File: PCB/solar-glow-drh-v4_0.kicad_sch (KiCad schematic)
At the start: 73 parts, among them J1 UPDI hdr, Q2 BSS138LT1G, SW2 LED master, U1 AVR64EA28 (VQFN28), U3 ADXL367, U5 NT3H2211, U6 TPS22917, U7 MB85RC512TY, U8 AEM10300, U9 TPS7A0233 (SOT23-5*)

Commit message: The fab package now says which board it is and how it is plated
Every one of the ten gerbers carried `%TF.ProjectId,solar-glow-drh-v4_0,<guid>,rev?*%`,
both .gbrjob files read "Revision": "rev?", and the stackup declared
`copper_finish "None"` -- on a board whose single most consequential fab instruction is
ENIG plus selective hard gold. The panel set was identical. Nothing failed: the fields
were simply blank, and blank is what a CAM operator reads when two zips from the same
project land in the same week.

The cause was one absence. The board had NO title block at all -- GetTitleBlock() returned
title, revision, date and company all empty -- and the schematic had none either.

  board + schematic: title block added (title / date / rev v4.0 / company)
  board stackup:     copper_finish "None" -> "ENIG"

Verified by plotting gerbers locally and reading back what the fab actually receives,
rather than trusting the edit:

  before   ProjectId ... rev?    Finish: None
  after    ProjectId ... v4.0    Finish: ENIG

CHECK [18] GATES BOTH, and gates the revision AGAINST THE FILENAME rather than a constant:
`...-v4_0.kicad_pcb` -> `v4.0`. The filename is already this project's revision of record
and PCB/ holds exactly one board, so a v5 rename now fails this check until the title
block follows it. Negative-tested three ways -- clean on the fixed board, 2 errors on the
exact pre-fix state (blank rev + finish None), 1 error on a rev/filename mismatch -- with
the board restored byte-identical afterward.

ON FINISH, and why ENIG alone is the right value: `copper_finish` is one field and cannot
express "ENIG plus selective hard gold on a named set of pads". ENIG is the base finish and
belongs there; the gold set lives where it can be DRAWN and GATED -- the User.1 plating
artwork generated by scripts/mask_art.py and checked by [14]. Check [18] only insists the
field is not blank, because the moment it tries to encode the special request it becomes a
second home for it.

Also cor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
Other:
- company: (none) -> Devin R. Horowitz
- title: (none) -> SOLAR-GLOW · DRH
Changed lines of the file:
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@@
 	(generator_version "10.0")
 	(paper "A4")
+	(title_block
+		(title "SOLAR-GLOW · DRH")
+		(date "2026-08-04")
+		(rev "v4.0")
+		(company "Devin R. Horowitz")
+	)
 	(no_connect
 		(at 410.21 139.7)

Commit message: The supercap lands pointed at a library that does not exist
SC1-SC4 linked to `Downloads:SCHURTER_SCPC_*` in BOTH the board and the schematic.
PCB/fp-lib-table registers exactly one library, `solarglow`. So the link never
resolved, "Update Footprints from Library" had nothing valid to pull, and the
corrected footprints in PCB/solarglow.pretty/ were unreachable from the board.

That is why correcting the library never reached the board, and why the land is
still wrong on three of four caps.

RELINKED, board and schematic together so schematic parity holds:
  SC1, SC3  Downloads:SCHURTER_SCPC_SS17      -> solarglow:SCHURTER_SCPC_SS17
  SC2, SC4  Downloads:SCHURTER_SCPC_WS17-mod2 -> solarglow:SCHURTER_SCPC_WS17
(`WS17-mod2` has no library counterpart; WS17 is the datasheet-correct land.)
Relinking moves NO copper -- the embedded pads stay until KiCad is told to update.

THE LIBRARY FOOTPRINTS WERE NOT SAFE TO LINK, and this fixes that. They were pad
geometry references, not usable footprints. Each gap would have bitten on the first
"Update Footprints from Library":

  - pads carried F.Paste. The board's carry B.Cu + B.Mask only, deliberately: these
    are hand-soldered under-body lands and PCB/README.md:497 warns that reflowing
    paste under them is "enough solder volume to float the part". Removed.
  - `(attr smd)` only, where the board has `exclude_from_pos_files exclude_from_bom`.
    Updating would have put four supercaps back into the CPL and the BOM -- the exact
    defect check [15] was written after. Set to match.
  - no 3D model. Updating would have stripped SCHURTER_SCPC_*.step, breaking checks
    [5]/[10], the renders and interference_drc. Added, with the board's own rotation.

They already carried the full F.Fab body, end-tab outlines, silk polarity mark and
courtyard -- an earlier "0 graphics" reading here was a broken regex, not a real gap.

KiCad loads both: pads at the datasheet positions, one model each, attrs 0xe.
Library files are LF, not CRLF li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
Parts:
- SC1, SC3: footprint Downloads:SCHURTER_SCPC_SS17 -> solarglow:SCHURTER_SCPC_SS17
- SC2, SC4: footprint Downloads:SCHURTER_SCPC_WS17-mod2 -> solarglow:SCHURTER_SCPC_WS17
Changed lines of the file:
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@@
 			)
 		)
-		(property "Footprint" "Downloads:SCHURTER_SCPC_WS17-mod2"
+		(property "Footprint" "solarglow:SCHURTER_SCPC_WS17"
 			(at 91.01 73.66 0)
 			(show_name no)
@@
 			)
 		)
-		(property "Footprint" "Downloads:SCHURTER_SCPC_SS17"
+		(property "Footprint" "solarglow:SCHURTER_SCPC_SS17"
 			(at 91.01 93.98 0)
 			(show_name no)
@@
 			)
 		)
-		(property "Footprint" "Downloads:SCHURTER_SCPC_SS17"
+		(property "Footprint" "solarglow:SCHURTER_SCPC_SS17"
 			(at 91.01 53.34 0)
 			(show_name no)
@@
 			)
 		)
-		(property "Footprint" "Downloads:SCHURTER_SCPC_WS17-mod2"
+		(property "Footprint" "solarglow:SCHURTER_SCPC_WS17"
 			(at 91.01 114.3 0)
 			(show_name no)

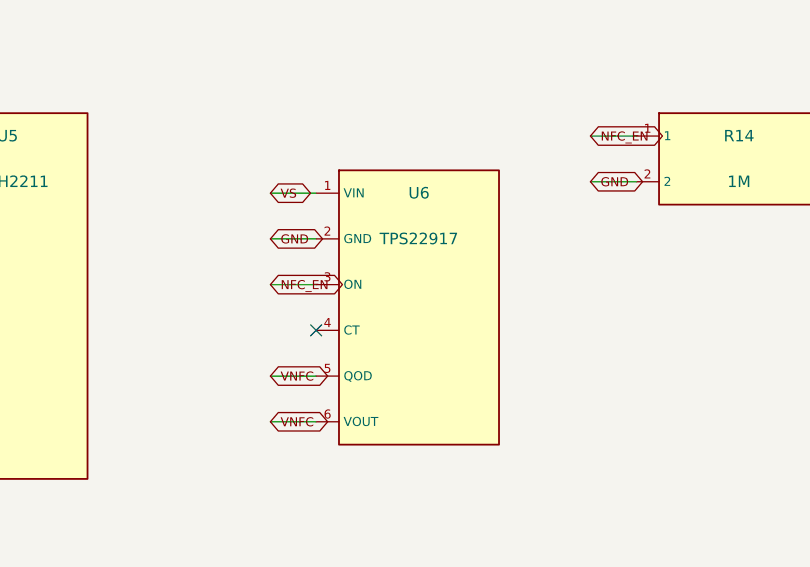
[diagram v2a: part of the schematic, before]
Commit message: U6 -> TPS22919 in the schematic, and the firmware constant that had to move with it
DELIBERATELY RED: check [3] now reports one error, U6's footprint
differing between schematic and board.  That is this change, not a
regression -- the schematic says SC-70-6 and the board still says
SOT-23-6, and only a KiCad "update PCB from schematic" can close it.
The repo's own note says as much: commit board and schematic together or
update-from-schematic will fight you.  The board half is DRH's KiCad
session; this is everything that can land ahead of it.

Why TPS22919 at all.  The objection was its 8 uA ON-state IQ against the
917's 0.5 uA, and it does not survive contact with the duty cycle:
nfc_provision_default() runs ONCE at cold boot (main.c:435), re-boots
exit early on the CC check, and FD-wake works with VCC gated off.  The
single provisioning window is ~157 ms -- 19 NDEF blocks, each 1.7 ms of
100 kHz bus plus the 6 ms NFC_EEPROM_WR_MS settle, plus the CC block --
so the IQ delta costs 7.5 uA x 3.3 V x 0.157 s = 3.9 uJ ONCE, EVER.
Against 9.8 J spendable that is 0.00004%, or 0.44 s of ordinary ~2.7 uA
dark standby.

The term that does run continuously goes the other way: ISD 10 nA -> 2 nA
typ, and on guaranteed numbers at 25 C it is <=20 nA against <=100 nA.
The 800 nA everyone quotes is the +125 C corner, where the 917 publishes
nothing at all -- so the "worse leakage" headline compares a specified
number against an absent one.  Annual saving beats the once-ever cost by
~200,000x.

It is pin-for-pin on every net we use.  Pin 4 goes CT-float -> NC-float
(we already floated CT, so the adjustable ramp was never in use), and
QOD->VOUT is explicitly sanctioned with the internal 24 ohm.  So the
schematic edit is properties plus one pin NAME; no pin numbers, no
positions, no wires moved.  ERC is unchanged at 3 pre-existing
isolated_pin_label warnings.  CRLF preserved (26153, zero bare LF).

Firmware co-requisite, landed here because it is safe for BOTH parts:
NFC_SOFTSTART_US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
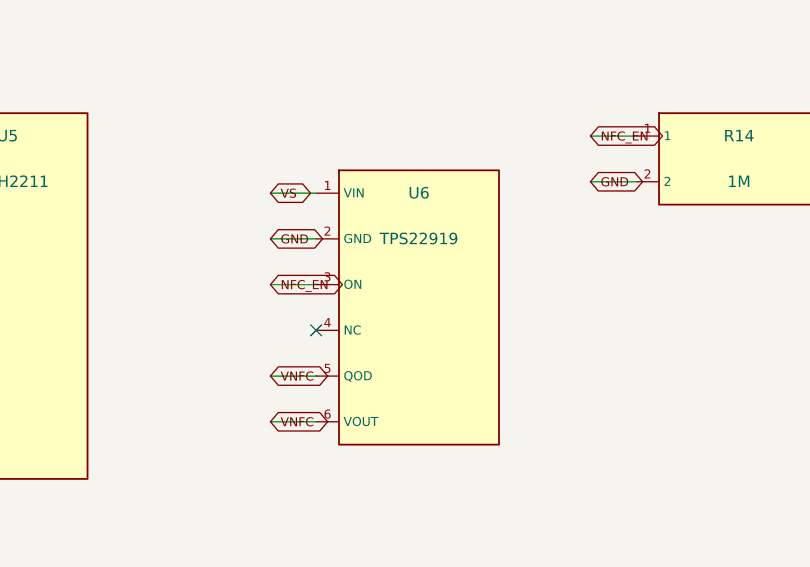
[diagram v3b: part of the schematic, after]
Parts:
- U6: value TPS22917 -> TPS22919; footprint Package_TO_SOT_SMD:SOT-23-6 -> Package_TO_SOT_SMD:SOT-363_SC-70-6; MPN TPS22917DBVT -> TPS22919DCKR
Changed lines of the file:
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@@
 			)
 		)
-		(property "Value" "TPS22917"
+		(property "Value" "TPS22919"
 			(at 661.67 81.28 0)
 			(show_name no)
@@
 			)
 		)
-		(property "Footprint" "Package_TO_SOT_SMD:SOT-23-6"
+		(property "Footprint" "Package_TO_SOT_SMD:SOT-363_SC-70-6"
 			(at 661.67 86.36 0)
 			(hide yes)
@@
 			)
 		)
-		(property "Datasheet" "datasheets/U6  TPS22917DBVT  $1.14.pdf"
+		(property "Datasheet" "SLVSEN5B"
 			(at 650.24 76.2 0)
 			(hide yes)
@@
 			)
 		)
-		(property "Description" "NFC VNFC high-side load switch - TPS22917 ultra-low leakage (ISD 10nA typ vs 918's 0.5uA/3.5uA max); pin-identical to TPS22918, CT float + QOD->VOUT sanctioned; active-HIGH ON (NOT the 917L)"
+		(property "Description" "NFC VNFC high-side load switch - TPS22919 (SC-70-6). ISD 2nA typ / 20nA max @25C vs the 917's 10nA typ / 100nA max, so better where the card lives; its 800nA max applies only at +125C, where the 917 specifies nothing at all. IQ 8uA typ while ON is a one-shot, not a standing cost: provisioning runs once at cold boot (~157ms), i.e. 3.9uJ against a 9.8J tank. Pin-for-pin with the 917 on every net used - pin4 CT-float becomes NC-float, QOD->VOUT sanctioned (internal 24 ohm), active-HIGH ON. Losses: no reverse-current blocking, and a fixed 1.75ms ramp (NFC_SOFTSTART_US raised to 2000). AEC-Q100 exists as TPS22919QDCKRQ1; the 917 has no -Q1 in any package."
 			(at 650.24 76.2 0)
 			(hide yes)
@@
 			)
 		)
-		(property "MPN" "TPS22917DBVT"
+		(property "MPN" "TPS22919DCKR"
 			(at 650.24 76.2 0)
 			(hide yes)
